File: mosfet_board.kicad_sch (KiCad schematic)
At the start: 18 parts, among them J1 Conn_01x07_Pin, J2 Conn_01x04_Pin, Q1 IRF510N, Q2 IRF510N, Q3 IRF510N, Q4 IRFZ44N

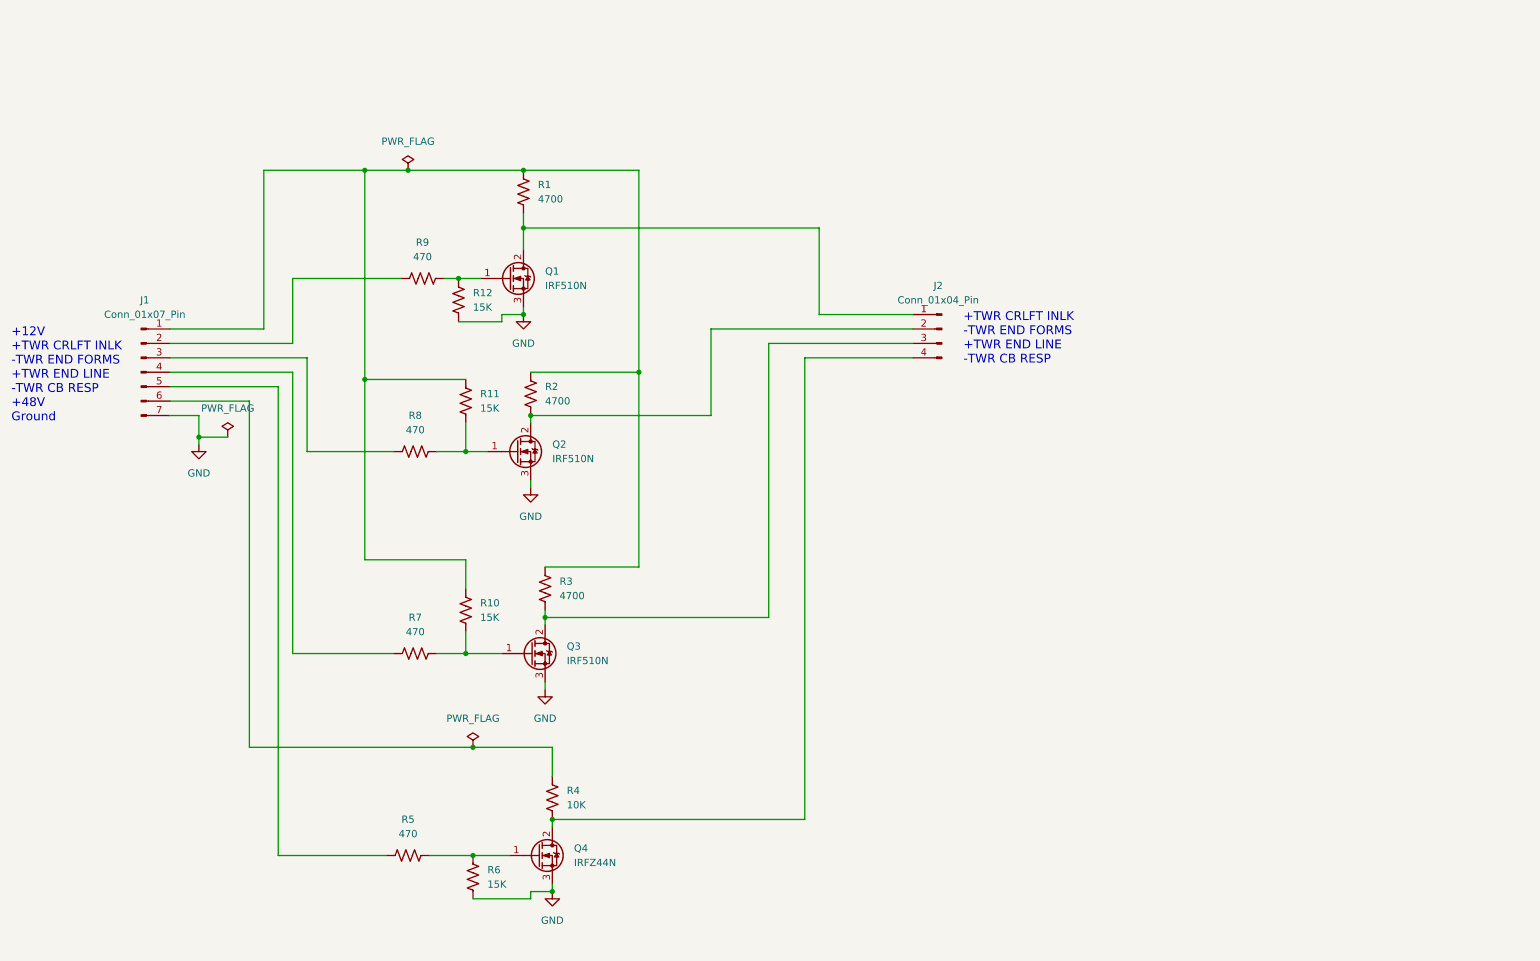
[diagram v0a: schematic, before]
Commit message: Version adding support for APL (988) typeball
User can switch between the normal console typeball (969) used with the 1130 and the special APL typeball 988 when booting and using the APL for 1130 software.
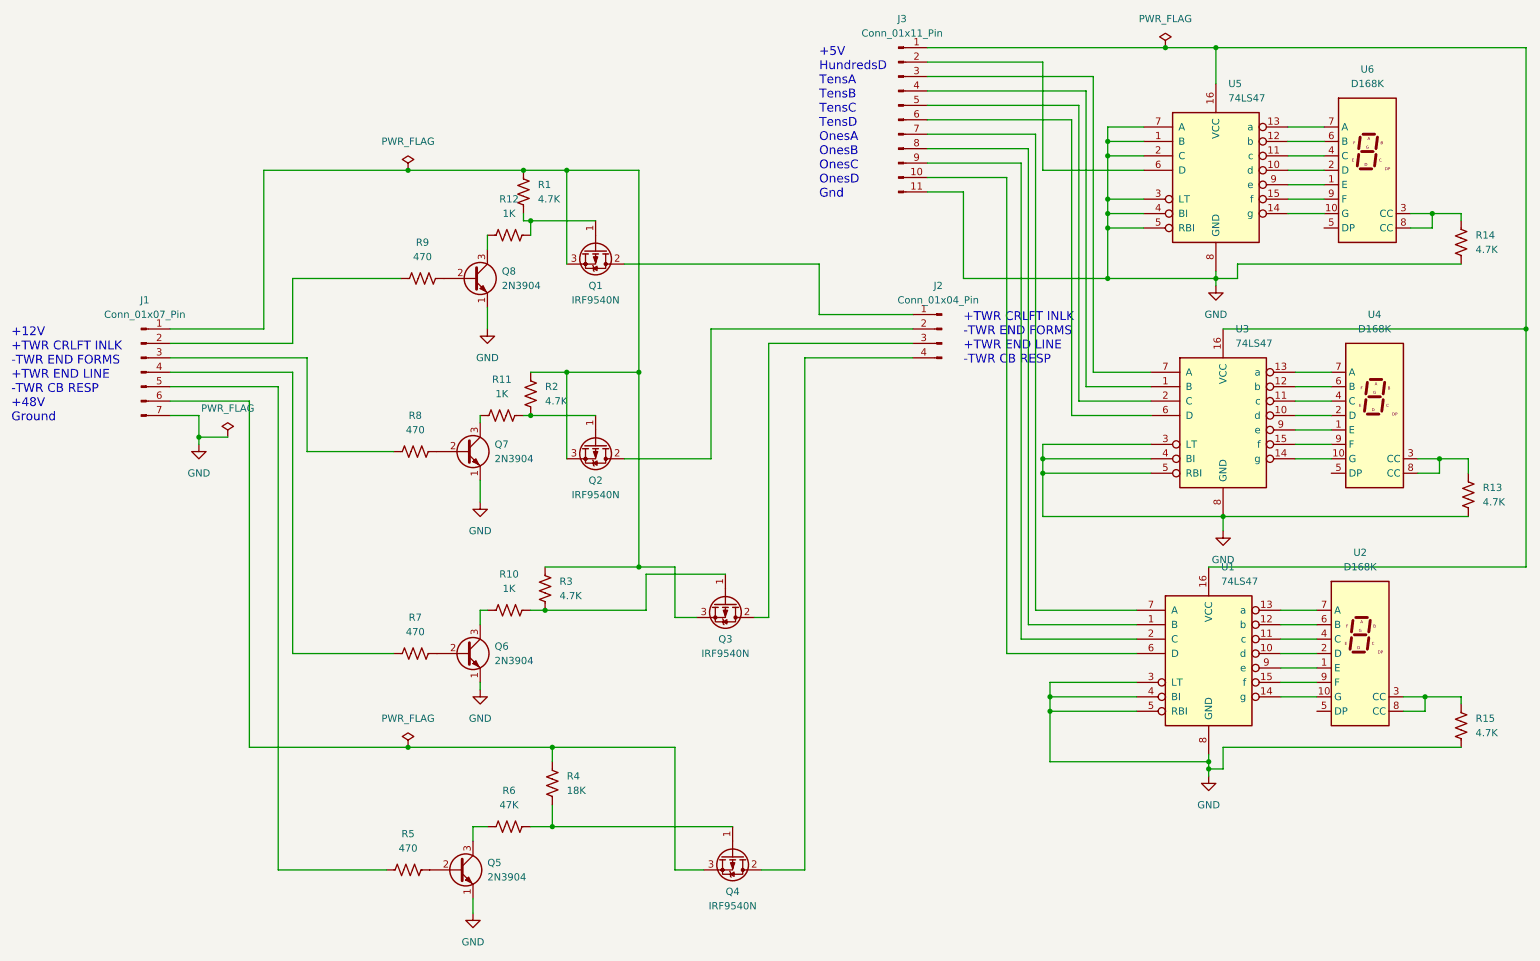
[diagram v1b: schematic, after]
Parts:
- added J3: Conn_01x11_Pin, symbol Connector:Conn_01x11_Pin
- added Q5, Q6, Q7, Q8: 2N3904, Package_TO_SOT_THT:TO-92_Inline, symbol Transistor_BJT:2N3904
- added R13, R14, R15: 4.7K, symbol Device:R_US
- added U1, U3, U5: 74LS47, symbol 74xx:74LS47
- added U2, U4, U6: D168K, Display_7Segment:D1X8K, symbol Display_Character:D168K
- Q1, Q2, Q3: value IRF510N -> IRF9540N; symbol Transistor_FET:IRF540N -> Transistor_FET:IRF9540N
- Q4: value IRFZ44N -> IRF9540N; symbol Transistor_FET:IRF540N -> Transistor_FET:IRF9540N
- R1, R2, R3: value 4700 -> 4.7K
- R10, R11, R12: value 15K -> 1K
- R4: value 10K -> 18K
- R6: value 15K -> 47K
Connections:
- net GND: now also J3.11 (Pin_11), Q5.1 (E), Q6.1 (E), Q7.1 (E), Q8.1 (E), R13.2, R14.2, R15.2, U1.3 (LT), U1.4 (BI), U1.5 (RBI), U1.8 (GND), U3.3 (LT), U3.4 (BI), U3.5 (RBI), U3.8 (GND), U5.1 (B), U5.2 (C), U5.3 (LT), U5.4 (BI), U5.5 (RBI), U5.7 (A), U5.8 (GND); no longer Q1.3 (S), Q2.3 (S), Q3.3 (S), Q4.3 (S), R12.2, R6.2
- net at Q2.1 (G), R11.2: now also R2.2; no longer R8.2
- net at J2.2 (Pin_2), Q2.2 (D): no longer R2.2
- net at J2.1 (Pin_1), Q1.2 (D): no longer R1.2
- net at J2.3 (Pin_3), Q3.2 (D): no longer R3.2
- net at J2.4 (Pin_4), Q4.2 (D): no longer R4.2
- net at J1.1 (Pin_1), R1.1, R2.1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: now also Q1.3 (S), Q2.3 (S), Q3.3 (S); no longer R10.1, R11.1
- net at Q3.1 (G), R10.2: now also R3.2; no longer R7.2
- net at J1.6 (Pin_6), R4.1: now also Q4.3 (S)
- new net: Q4.1 (G), R4.2, R6.2
- new net: Q5.2 (B), R5.2
- new net: Q5.3 (C), R6.1
- new net: U3.9 (e), U4.1 (E)
- new net: U3.14 (g), U4.10 (G)
- new net: U3.10 (d), U4.2 (D)
- new net: R13.1, U4.3 (CC), U4.8 (CC)
- new net: U3.11 (c), U4.4 (C)
- new net: U3.12 (b), U4.6 (B)
- new net: U3.13 (a), U4.7 (A)
- new net: U3.15 (f), U4.9 (F)
- new net: Q6.2 (B), R7.2
- new net: Q6.3 (C), R10.1
- new net: J3.8 (Pin_8), U1.1 (B)
- new net: U1.10 (d), U2.2 (D)
- new net: U1.11 (c), U2.4 (C)
- new net: U1.12 (b), U2.6 (B)
- new net: U1.13 (a), U2.7 (A)
- new net: U1.14 (g), U2.10 (G)
- new net: U1.15 (f), U2.9 (F)
- new net: J3.1 (Pin_1), U1.16 (VCC), U3.16 (VCC), U5.16 (VCC)
- new net: J3.9 (Pin_9), U1.2 (C)
- new net: J3.10 (Pin_10), U1.6 (D)
- new net: J3.7 (Pin_7), U1.7 (A)
- new net: U1.9 (e), U2.1 (E)
- new net: Q7.2 (B), R8.2
- new net: U5.10 (d), U6.2 (D)
- new net: U5.11 (c), U6.4 (C)
- new net: U5.12 (b), U6.6 (B)
- new net: U5.13 (a), U6.7 (A)
- new net: U5.14 (g), U6.10 (G)
- new net: U5.15 (f), U6.9 (F)
- new net: J3.2 (Pin_2), U5.6 (D)
- new net: U5.9 (e), U6.1 (E)
- new net: Q1.1 (G), R1.2, R12.2
- new net: Q8.2 (B), R9.2
- new net: Q8.3 (C), R12.1
- new net: R14.1, U6.3 (CC), U6.8 (CC)
- new net: J3.3 (Pin_3), U3.7 (A)
- new net: J3.4 (Pin_4), U3.1 (B)
- new net: J3.5 (Pin_5), U3.2 (C)
- new net: J3.6 (Pin_6), U3.6 (D)
- new net: R15.1, U2.3 (CC), U2.8 (CC)
- new net: Q7.3 (C), R11.1
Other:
- note added: "+5V HundredsD TensA TensB TensC TensD OnesA OnesB OnesC OnesD Gnd"
- moved on the sheet: Q1, Q2, Q3, Q4, R5
